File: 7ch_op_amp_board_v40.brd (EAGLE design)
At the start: 10.5 x 15.2 mm, 4 parts

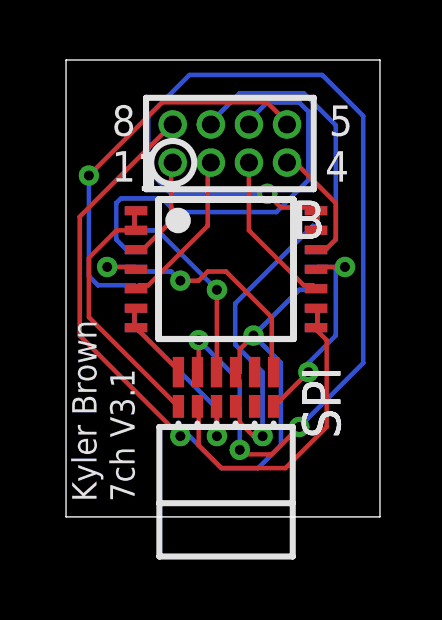
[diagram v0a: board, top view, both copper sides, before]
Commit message: Replace connector with through-holes
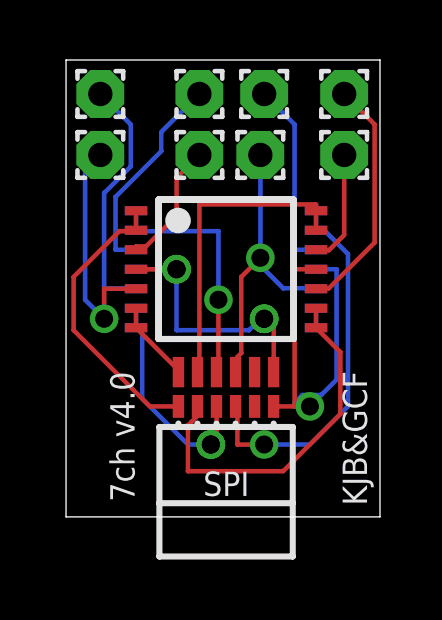
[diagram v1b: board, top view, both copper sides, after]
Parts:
- removed B: (no value), kjbrown:853-PPP-8
- added PAD1, PAD2, PAD3, PAD4, PAD5, PAD6, PAD7, PAD8: (no value), wirepad:1,6/0,8
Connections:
- removed net N$15: 2.3, B.P$5
- removed net N$16: 2.5, B.P$6
- removed net N$17: 2.10, B.P$7
- new net N$21: 2.10, PAD7.1
- new net N$22: 2.5, PAD6.1
- new net N$23: 2.3, PAD5.1
- net GND: now also PAD8.1; no longer B.P$8
- net N$11: now also 1.5, PAD2.1; no longer 1.3, B.P$1
- net N$12: now also 1.10, PAD3.1; no longer 1.5, B.P$2
- net N$13: now also 1.12, PAD4.1; no longer 1.10, B.P$3
- net N$8: now also 1.3, PAD1.1; no longer 1.12, B.P$4
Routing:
- net N$7: track 35.9 -> 10.4 mm, vias 4 -> 0
- net GND: track 25.5 -> 10.1 mm, vias 2 -> 1
- net N$16: track 13.9 -> 0.00 mm, vias 0 -> 1
- net N$15: track 13.1 -> 0.00 mm
- net N$17: track 9.68 -> 0.00 mm
- net N$23: track 0.00 -> 8.35 mm
- net N$22: track 0.00 -> 7.03 mm
- net N$21: track 0.00 -> 6.33 mm
- net V-: track 7.52 -> 13.7 mm, vias 2 -> 0
- net N$11: track 3.52 -> 8.00 mm, vias 0 -> 1
- net N$12: track 5.41 -> 7.97 mm
- net N$5: track 10.9 -> 12.7 mm
- net N$9: track 10.6 -> 12.2 mm
- net N$13: track 5.31 -> 3.83 mm
- net N$4: track 6.95 -> 8.27 mm
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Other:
- board text added: "7ch v4.0"
- board text added: "KJB&GCF"
- board text removed: "1"
- board text removed: "2"
- board text removed: "4"
- board text removed: "5"
- board text removed: "7ch V3.1"
- board text removed: "8"
- board text removed: "B"
- board text removed: "Kyler Brown"
